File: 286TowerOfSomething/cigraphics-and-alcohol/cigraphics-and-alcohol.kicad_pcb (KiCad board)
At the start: 2 copper layers, 2 parts, among them J1 Bus_ISA_16bit, U1 TVGA9000I-3

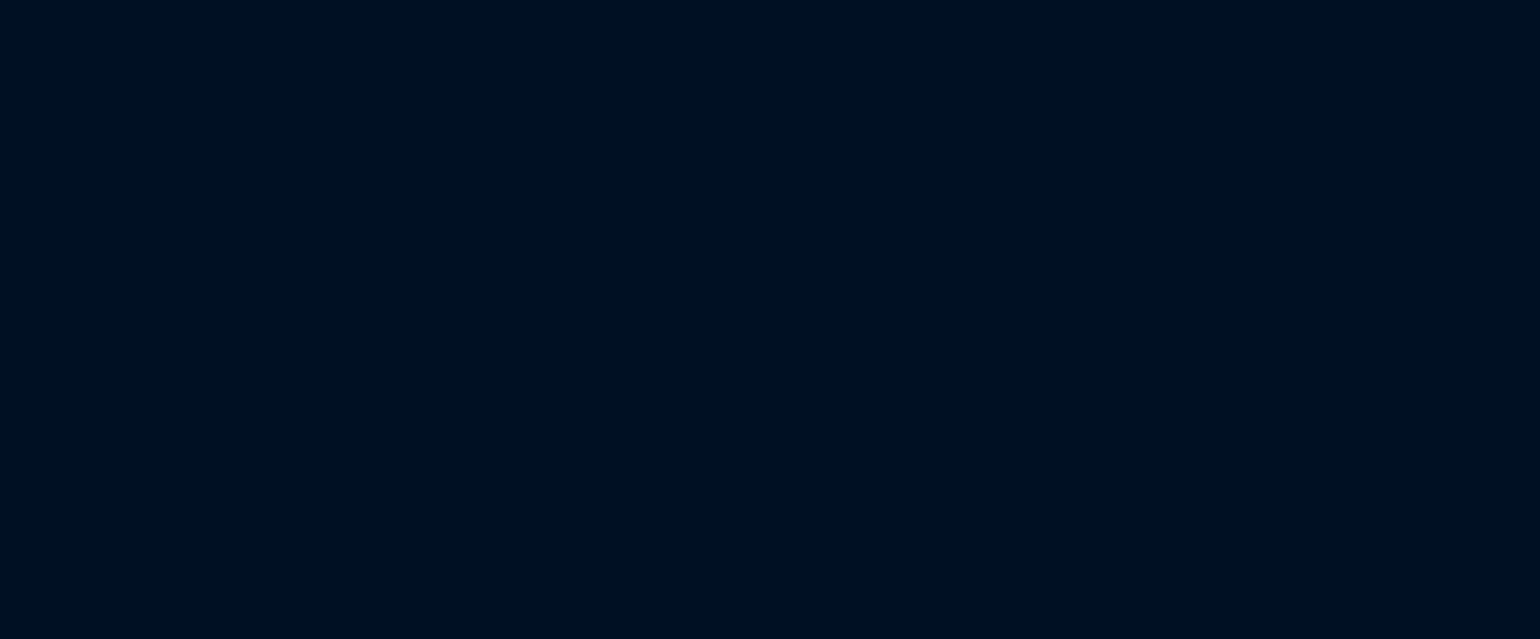
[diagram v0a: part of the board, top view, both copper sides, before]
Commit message: Adding RAM to cigraphics-and-alcohol
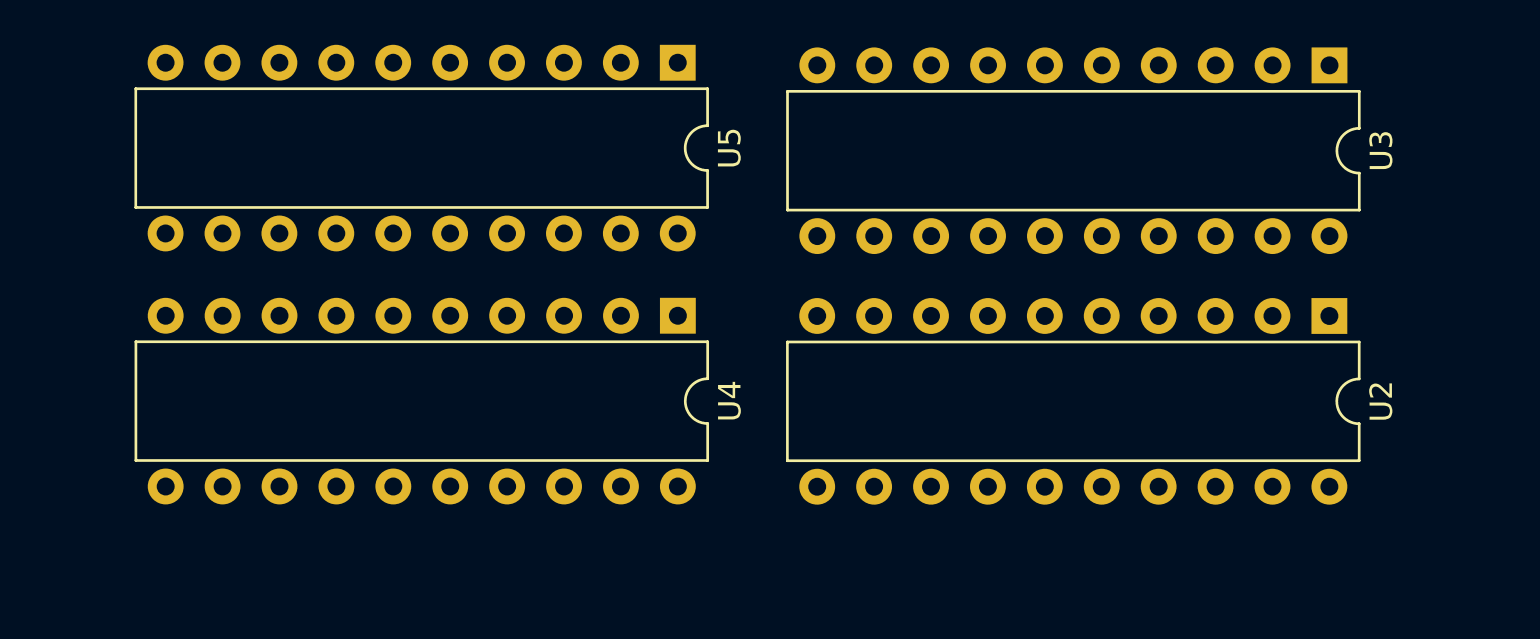
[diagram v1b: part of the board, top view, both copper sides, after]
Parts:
- added U2: MCM514256AP, Package_DIP:DIP-20_W7.62mm, F.Cu at (167.6, 32.8)
- added U3: MCM514256AP, Package_DIP:DIP-20_W7.62mm, F.Cu at (167.6, 21.6)
- added U4: MCM514256AP, Package_DIP:DIP-20_W7.62mm, F.Cu at (138.6, 32.8)
- added U5: MCM514256AP, Package_DIP:DIP-20_W7.62mm, F.Cu at (138.6, 21.5)
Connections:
- U1 pad 52: unconnected-(U1B-MAA0-Pad52) -> /RAM/MAA0
- U1 pad 53: unconnected-(U1B-MAA1-Pad53) -> /RAM/MAA1
- U1 pad 54: unconnected-(U1B-MAA2-Pad54) -> /RAM/MAA2
- U1 pad 55: unconnected-(U1B-MAA3-Pad55) -> /RAM/MAA3
- U1 pad 56: unconnected-(U1B-MAA4-Pad56) -> /RAM/MAA4
- U1 pad 57: unconnected-(U1B-MAA5-Pad57) -> /RAM/MAA5
- U1 pad 59: unconnected-(U1B-MAA6-Pad59) -> /RAM/MAA6
- U1 pad 60: unconnected-(U1B-MAA7-Pad60) -> /RAM/MAA7
- U1 pad 61: unconnected-(U1B-MAA8-Pad61) -> /RAM/MAA8
- U1 pad 64: unconnected-(U1B-MD0-Pad64) -> /RAM/MD0
- U1 pad 65: unconnected-(U1B-MD1-Pad65) -> /RAM/MD1
- U1 pad 66: unconnected-(U1B-MD2-Pad66) -> /RAM/MD2
- U1 pad 67: unconnected-(U1B-MD3-Pad67) -> /RAM/MD3
- U1 pad 68: unconnected-(U1B-MD4-Pad68) -> /RAM/MD4
- U1 pad 70: unconnected-(U1B-MD5-Pad70) -> /RAM/MD5
- U1 pad 71: unconnected-(U1B-MD6-Pad71) -> /RAM/MD6
- U1 pad 72: unconnected-(U1B-MD7-Pad72) -> /RAM/MD7
- U1 pad 73: unconnected-(U1B-MAB0-Pad73) -> /RAM/MAB0
- U1 pad 74: unconnected-(U1B-MAB1-Pad74) -> /RAM/MAB1
- U1 pad 75: unconnected-(U1B-MAB2-Pad75) -> /RAM/MAB2
- U1 pad 76: unconnected-(U1B-MAB3-Pad76) -> /RAM/MAB3
- U1 pad 77: unconnected-(U1B-MAB4-Pad77) -> /RAM/MAB4
- U1 pad 78: unconnected-(U1B-MAB5-Pad78) -> /RAM/MAB5
- U1 pad 82: unconnected-(U1B-MAB6-Pad82) -> /RAM/MAB6
- U1 pad 83: unconnected-(U1B-MAB7-Pad83) -> /RAM/MAB7
- U1 pad 84: unconnected-(U1B-MAB8-Pad84) -> /RAM/MAB8
- U1 pad 85: unconnected-(U1B-~{CAS}-Pad85) -> /RAM/~{CAS}
- U1 pad 86: unconnected-(U1B-~{RAS}-Pad86) -> /RAM/~{RAS}
- U1 pad 87: unconnected-(U1B-~{WE2}-Pad87) -> /RAM/~{WE2}
- U1 pad 88: unconnected-(U1B-~{WE0}-Pad88) -> /RAM/~{WE0}
- U1 pad 89: unconnected-(U1B-MD16-Pad89) -> /RAM/MD16
- U1 pad 90: unconnected-(U1B-MD17-Pad90) -> /RAM/MD17
- U1 pad 91: unconnected-(U1B-MD18-Pad91) -> /RAM/MD18
- U1 pad 92: unconnected-(U1B-MD19-Pad92) -> /RAM/MD19
- U1 pad 93: unconnected-(U1B-MD20-Pad93) -> /RAM/MD20
- U1 pad 94: unconnected-(U1B-MD21-Pad94) -> /RAM/MD21
- U1 pad 95: unconnected-(U1B-MD22-Pad95) -> /RAM/MD22
- U1 pad 96: unconnected-(U1B-MD23-Pad96) -> /RAM/MD23

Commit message: Adding bracket to graphics card
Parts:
- added C1: 100n, Capacitor_SMD:C_0603_1608Metric_Pad1.08x0.95mm_HandSolder, F.Cu at (120.4, 60.2)
- added C10: 100n, Capacitor_SMD:C_0603_1608Metric_Pad1.08x0.95mm_HandSolder, F.Cu at (145.8, 127.0)
- added C11: 100n, Capacitor_SMD:C_0603_1608Metric_Pad1.08x0.95mm_HandSolder, F.Cu at (167.6, 108.7)
- added C12: 100n, Capacitor_SMD:C_0603_1608Metric_Pad1.08x0.95mm_HandSolder, F.Cu at (167.6, 94.2)
- added C13: 100n, Capacitor_SMD:C_0603_1608Metric_Pad1.08x0.95mm_HandSolder, F.Cu at (167.6, 116.6)
- added C14: 100n, Capacitor_SMD:C_0603_1608Metric_Pad1.08x0.95mm_HandSolder, F.Cu at (137.9, 135.6)
- added C15: 22u, Capacitor_SMD:CP_Elec_5x5.3, F.Cu at (170.9, 124.5)
- added C16: 22u, Capacitor_SMD:CP_Elec_5x5.3, F.Cu at (128.5, 89.9)
- added C17: 10u, Capacitor_SMD:CP_Elec_5x5.3, F.Cu at (131.8, 129.3)
- added C18: 100n, Capacitor_SMD:C_0603_1608Metric_Pad1.08x0.95mm_HandSolder, F.Cu at (135.9, 127.0)
- added C19: 10u, Capacitor_SMD:CP_Elec_5x5.3, F.Cu at (173.5, 115.1)
- added C2: 100n, Capacitor_SMD:C_0603_1608Metric_Pad1.08x0.95mm_HandSolder, F.Cu at (120.4, 71.6)
- added C20: 100n, Capacitor_SMD:C_0603_1608Metric_Pad1.08x0.95mm_HandSolder, F.Cu at (167.6, 113.3)
- added C21: 100n, Capacitor_SMD:C_0603_1608Metric_Pad1.08x0.95mm_HandSolder, F.Cu at (137.9, 127.0)
- added C22: 47n, Capacitor_SMD:C_0603_1608Metric_Pad1.08x0.95mm_HandSolder, F.Cu at (221.0, 105.4)
- added C23: 47n, Capacitor_SMD:C_0603_1608Metric_Pad1.08x0.95mm_HandSolder, F.Cu at (221.0, 102.9)
- added C24: 1u, Capacitor_SMD:C_0603_1608Metric_Pad1.08x0.95mm_HandSolder, F.Cu at (221.0, 100.3)
- added C25: 47n, Capacitor_SMD:C_0603_1608Metric_Pad1.08x0.95mm_HandSolder, F.Cu at (221.0, 97.8)
- added C26: 47n, Capacitor_SMD:C_0603_1608Metric_Pad1.08x0.95mm_HandSolder, F.Cu at (221.0, 95.2)
- added C27: 47n, Capacitor_SMD:C_0603_1608Metric_Pad1.08x0.95mm_HandSolder, F.Cu at (221.0, 108.0)
- added C28: 470p, Capacitor_SMD:C_0603_1608Metric_Pad1.08x0.95mm_HandSolder, F.Cu at (166.2, 128.6)
- added C29: 47p, Capacitor_SMD:C_0603_1608Metric_Pad1.08x0.95mm_HandSolder, F.Cu at (166.2, 131.2)
- added C3: 100n, Capacitor_SMD:C_0603_1608Metric_Pad1.08x0.95mm_HandSolder, F.Cu at (149.9, 59.4)
- added C30: 100p, Capacitor_SMD:C_0603_1608Metric_Pad1.08x0.95mm_HandSolder, F.Cu at (166.2, 133.7)
- added C31: 47p, Capacitor_SMD:C_0603_1608Metric_Pad1.08x0.95mm_HandSolder, F.Cu at (141.1, 82.8)
- added C32: 47p, Capacitor_SMD:C_0603_1608Metric_Pad1.08x0.95mm_HandSolder, F.Cu at (141.1, 85.3)
- added C33: 100n, Capacitor_SMD:C_0603_1608Metric_Pad1.08x0.95mm_HandSolder, F.Cu at (195.6, 85.6)
- added C4: 100n, Capacitor_SMD:C_0603_1608Metric_Pad1.08x0.95mm_HandSolder, F.Cu at (149.9, 70.9)
- added C5: 100n, Capacitor_SMD:C_0603_1608Metric_Pad1.08x0.95mm_HandSolder, F.Cu at (128.3, 121.2)
- added C6: 100n, Capacitor_SMD:C_0603_1608Metric_Pad1.08x0.95mm_HandSolder, F.Cu at (154.2, 88.9)
- added C7: 100n, Capacitor_SMD:C_0603_1608Metric_Pad1.08x0.95mm_HandSolder, F.Cu at (142.5, 88.9)
- added C8: 100n, Capacitor_SMD:C_0603_1608Metric_Pad1.08x0.95mm_HandSolder, F.Cu at (147.1, 88.9)
- added C9: 100n, Capacitor_SMD:C_0603_1608Metric_Pad1.08x0.95mm_HandSolder, F.Cu at (128.3, 95.8)
- added FB1: FerriteBead_Small, Inductor_SMD:L_0603_1608Metric_Pad1.05x0.95mm_HandSolder, F.Cu at (215.9, 100.3)
- added FB2: FerriteBead_Small, Inductor_SMD:L_0603_1608Metric_Pad1.05x0.95mm_HandSolder, F.Cu at (215.9, 102.9)
- added FB3: FerriteBead_Small, Inductor_SMD:L_0603_1608Metric_Pad1.05x0.95mm_HandSolder, F.Cu at (215.9, 105.4)
- added FB4: FerriteBead_Small, Inductor_SMD:L_0603_1608Metric_Pad1.05x0.95mm_HandSolder, F.Cu at (215.9, 97.8)
- added FB5: FerriteBead_Small, Inductor_SMD:L_0603_1608Metric_Pad1.05x0.95mm_HandSolder, F.Cu at (215.9, 95.2)
- added FB6: FerriteBead_Small, Inductor_SMD:L_0603_1608Metric_Pad1.05x0.95mm_HandSolder, F.Cu at (215.9, 108.0)
- added J2: VGA, Connector_Dsub:DSUB-15-HD_Female_Horizontal_P2.29x1.90mm_EdgePinOffset3.03mm_Housed_MountingHolesOffset4.94mm, F.Cu at (226.4, 98.2)
- added L1: 2.7u, Inductor_SMD:L_0603_1608Metric_Pad1.05x0.95mm_HandSolder, F.Cu at (137.9, 131.3)
- added L2: 2.7u, Inductor_SMD:L_0603_1608Metric_Pad1.05x0.95mm_HandSolder, F.Cu at (127.8, 126.0)
- added L3: 2.7u, Inductor_SMD:L_0603_1608Metric_Pad1.05x0.95mm_HandSolder, F.Cu at (167.6, 115.1)
- added R1: 150, Resistor_SMD:R_0603_1608Metric_Pad0.98x0.95mm_HandSolder, F.Cu at (167.6, 110.2)
- added R10: 4.7K, Resistor_SMD:R_0603_1608Metric_Pad0.98x0.95mm_HandSolder, F.Cu at (167.6, 99.1)
- added R11: 4.7K, Resistor_SMD:R_0603_1608Metric_Pad0.98x0.95mm_HandSolder, F.Cu at (167.6, 102.1)
- added R12: 4.7K, Resistor_SMD:R_0603_1608Metric_Pad0.98x0.95mm_HandSolder, F.Cu at (208.5, 69.3)
- added R13: 4.7K, Resistor_SMD:R_0603_1608Metric_Pad0.98x0.95mm_HandSolder, F.Cu at (207.4, 60.3)
- added R14: 4.7K, Resistor_SMD:R_0603_1608Metric_Pad0.98x0.95mm_HandSolder, F.Cu at (207.4, 62.8)
- added R15: 4.7K, Resistor_SMD:R_0603_1608Metric_Pad0.98x0.95mm_HandSolder, F.Cu at (207.4, 65.3)
- added R16: 33, Resistor_SMD:R_0603_1608Metric_Pad0.98x0.95mm_HandSolder, F.Cu at (135.6, 82.8)
- added R17: 33, Resistor_SMD:R_0603_1608Metric_Pad0.98x0.95mm_HandSolder, F.Cu at (145.4, 82.8)
- added R2: 4.7K, Resistor_SMD:R_0603_1608Metric_Pad0.98x0.95mm_HandSolder, F.Cu at (210.8, 100.3)
- added R3: 150, Resistor_SMD:R_0603_1608Metric_Pad0.98x0.95mm_HandSolder, F.Cu at (210.8, 97.8)
- added R4: 150, Resistor_SMD:R_0603_1608Metric_Pad0.98x0.95mm_HandSolder, F.Cu at (210.8, 95.2)
- added R5: 150, Resistor_SMD:R_0603_1608Metric_Pad0.98x0.95mm_HandSolder, F.Cu at (210.8, 108.0)
- added R6: 1K, Resistor_SMD:R_0603_1608Metric_Pad0.98x0.95mm_HandSolder, F.Cu at (166.2, 136.2)
- added R7: 100, Resistor_SMD:R_0603_1608Metric_Pad0.98x0.95mm_HandSolder, F.Cu at (166.2, 138.7)
- added R8: 4.7K, Resistor_SMD:R_0603_1608Metric_Pad0.98x0.95mm_HandSolder, F.Cu at (167.6, 95.8)
- added R9: 4.7K, Resistor_SMD:R_0603_1608Metric_Pad0.98x0.95mm_HandSolder, F.Cu at (208.5, 73.2)
- added SW1: SW_DIP_x05, Button_Switch_THT:SW_DIP_SPSTx05_Slide_9.78x14.88mm_W7.62mm_P2.54mm, F.Cu at (185.0, 62.2)
- added U6: SST39SF010, Package_DIP:DIP-32_W15.24mm, F.Cu at (180.3, 89.2)
- added U7: ~, pc-parts:PC_BRACKET_ISA_KEYSTONE_9200_Rev1_1, F.Cu at (208.3, 152.4)
- added Y1: 40.00 MHz, Crystal:Crystal_HC49-4H_Vertical, F.Cu at (142.0, 133.8)
- moved J1 43.2 mm to (208.3, 148.6)
- moved U4 39.7 mm to (146.7, 71.6)
- moved U2 39.7 mm to (175.8, 71.6)
- moved U3 39.6 mm to (175.7, 60.3)
- moved U1 39.6 mm to (147.9, 108.5)
- moved U5 39.6 mm to (146.7, 60.2)
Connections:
- net Net-(J1-BA01) renamed /A1
- net Net-(J1-BA02) renamed /A2
- net Net-(J1-BA03) renamed /A3
- net Net-(J1-BA04) renamed /A4
- net Net-(J1-BA05) renamed /A5
- net Net-(J1-BA06) renamed /A6
- net Net-(J1-BA07) renamed /A7
- net Net-(J1-BA08) renamed /A8
- net Net-(J1-BA09) renamed /A9
- net Net-(J1-BA10) renamed /A10
- net Net-(J1-BA11) renamed /A11
- net Net-(J1-BA12) renamed /A12
- net Net-(J1-BA13) renamed /A13
- net Net-(J1-BA14) renamed /A14
- J1 pad 1: unconnected-(J1-GND-Pad1) -> GND
- J1 pad 10: unconnected-(J1-GND-Pad10) -> GND
- J1 pad 11: unconnected-(J1-~{SMEMW}-Pad11) -> /~{MEMW}
- J1 pad 12: unconnected-(J1-~{SMEMR}-Pad12) -> /~{MEMR}
- J1 pad 13: unconnected-(J1-~{IOW}-Pad13) -> /~{IOW}
- J1 pad 14: unconnected-(J1-~{IOR}-Pad14) -> /~{IOR}
- J1 pad 19: unconnected-(J1-~{REFRESH}-Pad19) -> /~{REFRESH}
- J1 pad 2: unconnected-(J1-RESET-Pad2) -> /RESET
- J1 pad 28: unconnected-(J1-ALE-Pad28) -> /ALE
- J1 pad 29: unconnected-(J1-VCC-Pad29) -> +5V
- J1 pad 3: unconnected-(J1-+5V-Pad3) -> +5V
- J1 pad 30: unconnected-(J1-OSC-Pad30) -> /OSC
- J1 pad 31: unconnected-(J1-GND-Pad31) -> GND
- J1 pad 4: unconnected-(J1-IRQ2-Pad4) -> /IRQ
- J1 pad 63: unconnected-(J1-~{MEMCS16}-Pad63) -> /~{MEMCS16}
- J1 pad 78: unconnected-(J1-+5V-Pad78) -> +5V
- J1 pad 80: unconnected-(J1-GND-Pad80) -> GND
- U1 pad 1: unconnected-(U1D-AVSS2-Pad1) -> GND
- U1 pad 101: unconnected-(U1D-VSS-Pad101) -> GND
- U1 pad 102: unconnected-(U1A-~{MCS16}-Pad102) -> /~{MEMCS16}
- U1 pad 111: unconnected-(U1A-IRQ-Pad111) -> /IRQ_SW
- U1 pad 120: unconnected-(U1D-VDD-Pad120) -> +5V
- U1 pad 121: unconnected-(U1D-VSS-Pad121) -> GND
- U1 pad 122: unconnected-(U1D-VSS-Pad122) -> GND
- U1 pad 124: unconnected-(U1D-AVDD1-Pad124) -> Net-(U1D-AVDD1)
- U1 pad 125: unconnected-(U1C-VLF-Pad125) -> Net-(U1C-VLF)
- U1 pad 126: unconnected-(U1D-AVSS1-Pad126) -> GND
- U1 pad 128: unconnected-(U1D-DVSS1-Pad128) -> GND
- U1 pad 13: unconnected-(U1D-AVDD2-Pad13) -> Net-(C19-Pad1)
- U1 pad 130: unconnected-(U1D-DVDD1-Pad130) -> +5V
- U1 pad 131: unconnected-(U1D-XTL1-Pad131) -> Net-(U1D-XTL1)
- U1 pad 133: unconnected-(U1D-XTL2-Pad133) -> Net-(U1D-XTL2)
- U1 pad 134: unconnected-(U1D-VDD-Pad134) -> +5V
- U1 pad 143: unconnected-(U1D-VSS-Pad143) -> GND
- U1 pad 153: unconnected-(U1A-~{IOR}-Pad153) -> /~{IOR}
- U1 pad 154: unconnected-(U1A-~{IOW}-Pad154) -> Net-(U1A-~{IOW})
- U1 pad 155: unconnected-(U1A-~{MEMR}-Pad155) -> /~{MEMR}
- U1 pad 156: unconnected-(U1A-~{MEMW}-Pad156) -> /~{MEMW}
- U1 pad 158: unconnected-(U1A-ENMEM-Pad158) -> /~{REFRESH}
- U1 pad 160: unconnected-(U1D-VSS-Pad160) -> GND
- U1 pad 18: unconnected-(U1C-IRSET-Pad18) -> Net-(U1C-IRSET)
- U1 pad 19: unconnected-(U1D-VDD-Pad19) -> +5V
- U1 pad 2: unconnected-(U1C-B-Pad2) -> Net-(U1C-B)
- U1 pad 20: unconnected-(U1C-VREF-Pad20) -> +5V
- U1 pad 21: unconnected-(U1A-ALE-Pad21) -> /ALE
- U1 pad 23: unconnected-(U1D-VSS-Pad23) -> GND
- U1 pad 3: unconnected-(U1C-G-Pad3) -> Net-(U1C-G)
- U1 pad 33: unconnected-(U1C-RMD7-Pad33) -> Net-(U1C-RMD7)
- U1 pad 34: unconnected-(U1C-RMD6-Pad34) -> Net-(U1C-RMD6)
- U1 pad 35: unconnected-(U1C-RMD5-Pad35) -> Net-(U1C-RMD5)
- U1 pad 36: unconnected-(U1C-RMD4-Pad36) -> Net-(U1C-RMD4)
- U1 pad 37: unconnected-(U1C-RMD3-Pad37) -> Net-(U1C-RMD3)
- U1 pad 38: unconnected-(U1C-RMD2-Pad38) -> Net-(U1C-RMD2)
- U1 pad 39: unconnected-(U1C-RMD1-Pad39) -> Net-(U1C-RMD1)
- U1 pad 4: unconnected-(U1C-R-Pad4) -> Net-(U1C-R)
- U1 pad 40: unconnected-(U1D-VDD-Pad40) -> +5V
- U1 pad 41: unconnected-(U1D-VSS-Pad41) -> GND
- U1 pad 42: unconnected-(U1D-VSS-Pad42) -> GND
- U1 pad 43: unconnected-(U1C-RMD0-Pad43) -> Net-(U1C-RMD0)
- U1 pad 45: unconnected-(U1C-ROMCS-Pad45) -> Net-(U1C-ROMCS)
- U1 pad 46: unconnected-(U1C-MONITOR-Pad46) -> Net-(U1C-MONITOR)
- U1 pad 47: unconnected-(U1C-VSYNC-Pad47) -> Net-(U1C-VSYNC)
- U1 pad 48: unconnected-(U1C-HSYNC-Pad48) -> Net-(U1C-HSYNC)
- U1 pad 49: unconnected-(U1C-EVIDEO-Pad49) -> GND
- U1 pad 5: unconnected-(U1A-RESET-Pad5) -> Net-(U1A-RESET)
- U1 pad 50: unconnected-(U1C-EDCLK-Pad50) -> GND
- U1 pad 51: unconnected-(U1C-ESYNC-Pad51) -> +5V
- U1 pad 58: unconnected-(U1D-VSS-Pad58) -> GND
- U1 pad 6: unconnected-(U1D-AVDD2-Pad6) -> Net-(C19-Pad1)
- U1 pad 62: unconnected-(U1D-VDD-Pad62) -> +5V
- U1 pad 69: unconnected-(U1D-VDD-Pad69) -> +5V
- U1 pad 7: unconnected-(U1D-DVSS2-Pad7) -> GND
- U1 pad 79: unconnected-(U1D-VSS-Pad79) -> GND
- U1 pad 8: unconnected-(U1D-DVDD2-Pad8) -> +5V
- U1 pad 80: unconnected-(U1D-VSS-Pad80) -> GND
- U1 pad 81: unconnected-(U1D-VDD-Pad81) -> +5V
- U1 pad 85: /RAM/~{CAS} -> Net-(U1B-~{CAS})
- U1 pad 86: /RAM/~{RAS} -> Net-(U1B-~{RAS})
- U1 pad 97: unconnected-(U1C-ROMBA0-Pad97) -> Net-(U1C-ROMBA0)
- U1 pad 98: unconnected-(U1C-ROMCLK-Pad98) -> /OSC
- U2 pad 10: unconnected-(U2-VCC-Pad10) -> +5V
- U2 pad 16: Net-(U2-VSS) -> GND
- U2 pad 20: Net-(U2-VSS) -> GND
- U3 pad 10: unconnected-(U3-VCC-Pad10) -> +5V
- U3 pad 16: Net-(U3-VSS) -> GND
- U3 pad 20: Net-(U3-VSS) -> GND
- U4 pad 10: unconnected-(U4-VCC-Pad10) -> +5V
- U4 pad 16: Net-(U4-VSS) -> GND
- U4 pad 20: Net-(U4-VSS) -> GND
- U5 pad 10: unconnected-(U5-VCC-Pad10) -> +5V
- U5 pad 16: Net-(U5-VSS) -> GND
- U5 pad 20: Net-(U5-VSS) -> GND
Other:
- board outline added: 242.4 x 106.7 mm
